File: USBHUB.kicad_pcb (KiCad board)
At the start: 4 copper layers, 205 parts, among them J1 USB_C_Receptacle, Q1 SI3421DV, Q2 SI3421DV, U1 CYPD3177_24x, U10 TPS20xxC, U11 USB_3_Type_A_Molex_484080003, U12 TPS20xxC, U13 USB_3_Type_A_Molex_484080003, U14 TPS20xxC, U15 USB_3_Type_A_Molex_484080003, U16 CYUSB3304-68LTXx, U2 TPS54331, U3 TLV75733PDBV, U4 TPS56637RPAR, U5 TVS2200DRVx, U6 PI3USB302-Ax, U7 TUSB522Px, U8 USB_3_Type_A_Molex_484080003, U9 TPS20xxC, Y1 26MHz

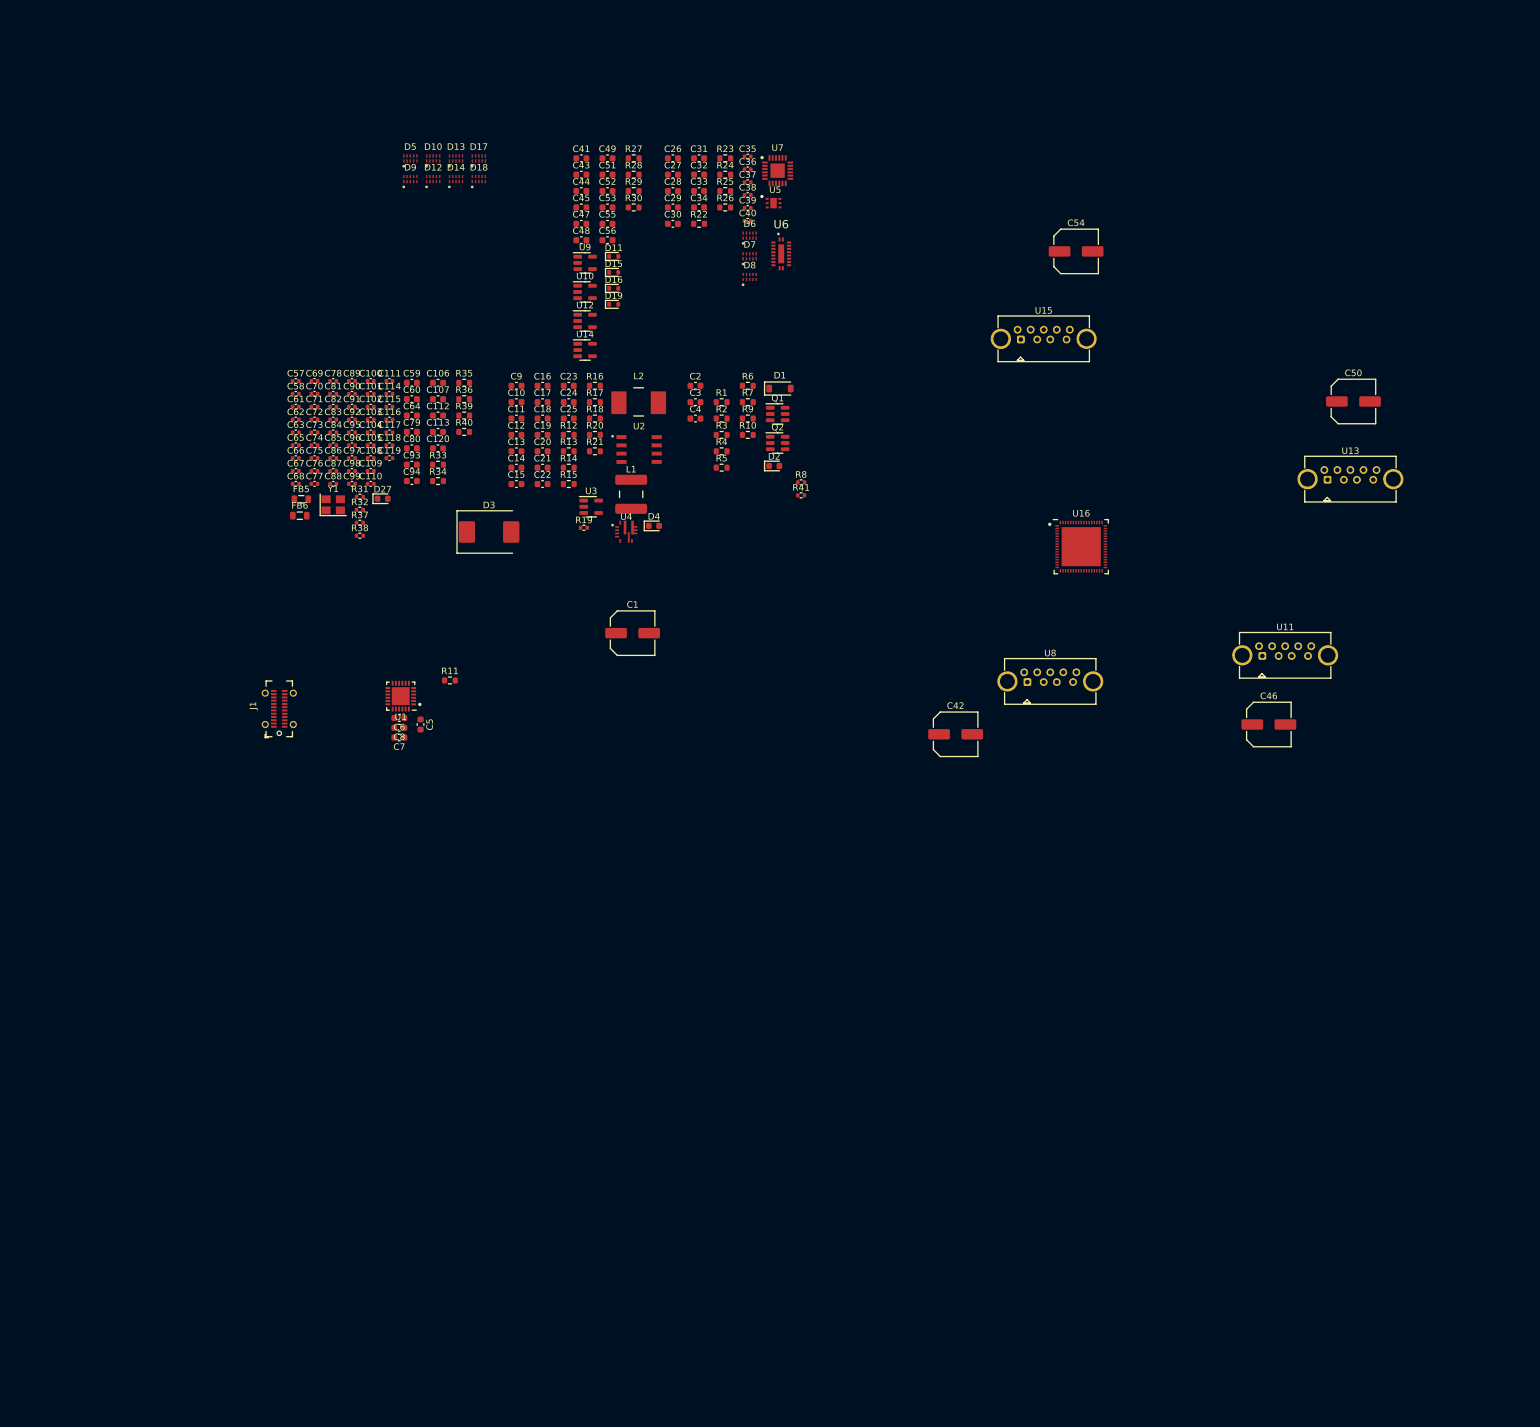
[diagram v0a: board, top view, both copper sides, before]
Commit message: fix symbols, route UFP DPs and voltage regs
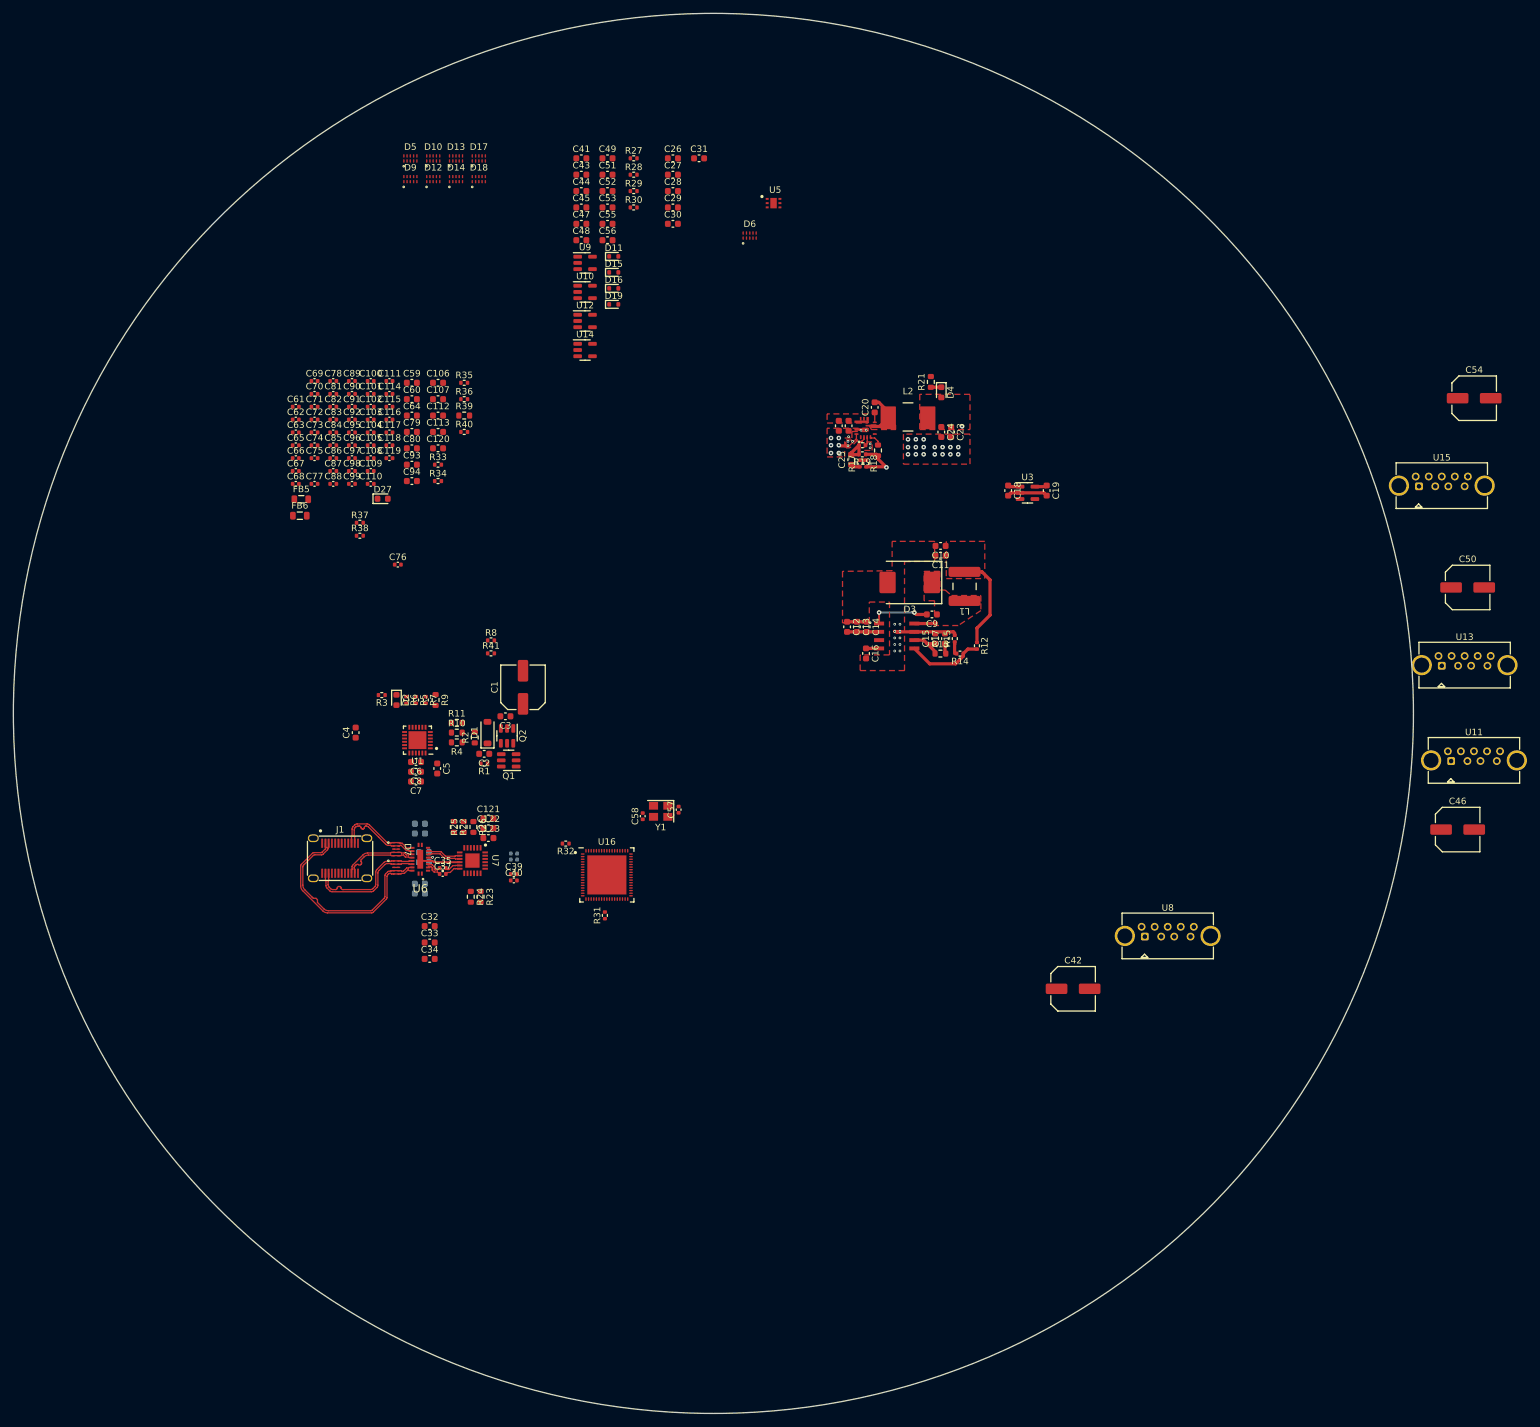
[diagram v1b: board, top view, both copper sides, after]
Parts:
- added C121: 10u, Capacitor_SMD:C_0603_1608Metric, F.Cu at (106.4, 131.9)
- added C122: 100n, Capacitor_SMD:C_0603_1608Metric, F.Cu at (106.4, 133.4)
- added C123: 100n, Capacitor_SMD:C_0603_1608Metric, F.Cu at (106.4, 134.9)
- added C124: 10u, Capacitor_SMD:C_0603_1608Metric, B.Cu at (95.9, 143.4)
- added C125: 100n, Capacitor_SMD:C_0603_1608Metric, B.Cu at (95.9, 141.9)
- added C126: 100n, Capacitor_SMD:C_0603_1608Metric, B.Cu at (95.9, 134.2)
- added C127: 10u, Capacitor_SMD:C_0603_1608Metric, B.Cu at (95.9, 132.7)
- added C128: 100n, Capacitor_SMD:C_0603_1608Metric, B.Cu at (96.5, 138.6)
- added C130: 10u, Capacitor_SMD:C_0603_1608Metric, B.Cu at (96.5, 137.1)
- C36, C38: moved to B.Cu
- J1: footprint CakeUSB:USB_C_Receptacle_GT-USB-7052 -> CakeUSB:USB_C_Receptacle_GT-USB-7028x
- R1, R12, R14, R15, R17, R18, R20, R27, R28, R29, R3, R30, R33, R34, R35, R36, R40, R5, R6, R7: footprint Resistor_SMD:R_0603_1608Metric -> Resistor_SMD:R_0402_1005Metric
- moved C32 122.3 mm to (97.4, 148.4)
- moved C33 122.3 mm to (97.4, 150.9)
- moved C34 122.3 mm to (97.4, 153.4)
- moved R23 119.2 mm to (105.2, 143.9), turned to -90 degrees
- moved C35 118.6 mm to (99.4, 139.5)
- moved R24 117.3 mm to (103.7, 143.9), turned to -90 degrees
- moved C37 115.8 mm to (99.4, 140.4)
- moved U7 115.6 mm to (104.0, 138.3), turned to -90 degrees
- moved C36 110.8 mm to (110.3, 137.3)
- moved C39 108.2 mm to (110.3, 140.4)
- moved U6 108.0 mm to (96.0, 138.2), turned to 180 degrees
- moved C38 107.9 mm to (110.3, 138.2)
- moved C40 107.2 mm to (110.3, 141.4)
- moved D7 105.8 mm to (92.3, 136.6), turned to -90 degrees
- moved D8 105.5 mm to (92.3, 139.4), turned to -90 degrees
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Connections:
- net Net-(D7-CH1) renamed /02 USB UFP/UFP_RX2-
- net Net-(D7-CH2) renamed /02 USB UFP/UFP_RX2+
- net Net-(D7-CH3) renamed /02 USB UFP/UFP_TX2-
- net Net-(D7-CH4) renamed /02 USB UFP/UFP_TX2+
- net Net-(D8-CH1) renamed /02 USB UFP/UFP_RX1-
- net Net-(D8-CH2) renamed /02 USB UFP/UFP_RX1+
- net Net-(D8-CH3) renamed /02 USB UFP/UFP_TX1-
- net Net-(D8-CH4) renamed /02 USB UFP/UFP_TX1+
- net Net-(U6-Tx+) renamed /02 USB UFP/UFP_TX+
- net Net-(U6-Tx-) renamed /02 USB UFP/UFP_TX-
- C35 pad 2: Net-(U7-TX1N) -> /02 USB UFP/UFP_TX_A_N
- C36 pad 1: Net-(U7-RX1N) -> /02 USB UFP/UFP_RX_B_N
- C36 pad 2: USB_UFP_TXN -> USB_UFP_RXN
- C37 pad 2: Net-(U7-TX1P) -> /02 USB UFP/UFP_TX_A_P
- C38 pad 1: Net-(U7-RX1P) -> /02 USB UFP/UFP_RX_B_P
- C38 pad 2: USB_UFP_TXP -> USB_UFP_RXP
- C39 pad 1: Net-(U7-TX2N) -> /02 USB UFP/UFP_TX_B_N
- C39 pad 2: USB_UFP_RXN -> USB_UFP_TXN
- C40 pad 1: Net-(U7-TX2P) -> /02 USB UFP/UFP_TX_B_P
- C40 pad 2: USB_UFP_RXP -> USB_UFP_TXP
- R23 pad 1: Net-(U7-EQ1) -> Net-(U7-EQ2)
- R24 pad 1: Net-(U7-OS2) -> Net-(U7-OS1)
- R25 pad 1: Net-(U7-OS1) -> Net-(U7-OS2)
- R26 pad 2: Net-(U7-EQ2) -> Net-(U7-EQ1)
- U6 pad 7: Net-(U6-Rx+) -> /02 USB UFP/UFP_RX+
- U6 pad 8: Net-(U6-Rx-) -> /02 USB UFP/UFP_RX-
- U7 pad 1: GND -> +3V3
- U7 pad 11: Net-(U7-TX2N) -> /02 USB UFP/UFP_TX_A_N
- U7 pad 12: Net-(U7-TX2P) -> /02 USB UFP/UFP_TX_A_P
- U7 pad 13: GND -> +3V3
- U7 pad 19: Net-(U6-Rx+) -> /02 USB UFP/UFP_TX_B_P
- U7 pad 20: Net-(U6-Rx-) -> /02 USB UFP/UFP_TX_B_N
- U7 pad 22: Net-(U7-TX1P) -> /02 USB UFP/UFP_RX_B_P
- U7 pad 23: Net-(U7-TX1N) -> /02 USB UFP/UFP_RX_B_N
- U7 pad 8: Net-(U7-RX1N) -> /02 USB UFP/UFP_RX-
- U7 pad 9: Net-(U7-RX1P) -> /02 USB UFP/UFP_RX+
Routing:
- net +5V: track 0.00 -> 33.3 mm, vias 0 -> 2
- net /02 USB UFP/UFP_TX1+: track 0.00 -> 32.7 mm
- net /02 USB UFP/UFP_TX1-: track 0.00 -> 32.4 mm
- net GND: track 0.00 -> 31.7 mm, vias 0 -> 41
- net /02 USB UFP/UFP_RX1+: track 0.00 -> 18.8 mm
- net /02 USB UFP/UFP_RX1-: track 0.00 -> 18.7 mm
- net +1V2: track 0.00 -> 14.5 mm
- net /02 USB UFP/UFP_RX2-: track 0.00 -> 13.5 mm
- net /02 USB UFP/UFP_RX2+: track 0.00 -> 13.4 mm
- net Net-(U2-VSENSE): track 0.00 -> 11.7 mm
- net /02 USB UFP/UFP_TX2-: track 0.00 -> 11.4 mm
- net /02 USB UFP/UFP_TX2+: track 0.00 -> 11.4 mm
- net Net-(U2-BOOT): track 0.00 -> 8.84 mm, vias 0 -> 2
- net Net-(U4-SW): track 0.00 -> 6.65 mm
- net Net-(U4-FB): track 0.00 -> 6.18 mm
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- added copper zone on F.Cu, net +1V2
- added copper zone on F.Cu, net +20V
- added copper zone on F.Cu, net +5V
- added copper zone on F.Cu, net GND
- added copper zone on In1.Cu, net GND
- added copper zone on F.Cu, net Net-(D3-K)
- added copper zone on F.Cu, net Net-(U4-SW)
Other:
- board outline added: 214.6 x 214.6 mm
